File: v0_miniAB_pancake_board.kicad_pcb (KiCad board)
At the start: 2 copper layers, 51 x 38.3 mm, 17 parts, among them J1 E_STEPPER, J10 FAN0_V_JUMPER, J11 FAN1_V_JUMPER, J12 RGB LED, J13 BLTOUCH, J2 HEATER, J3 THERM, J4 PART FAN, J5 PART FAN, J6 HOTEND FAN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

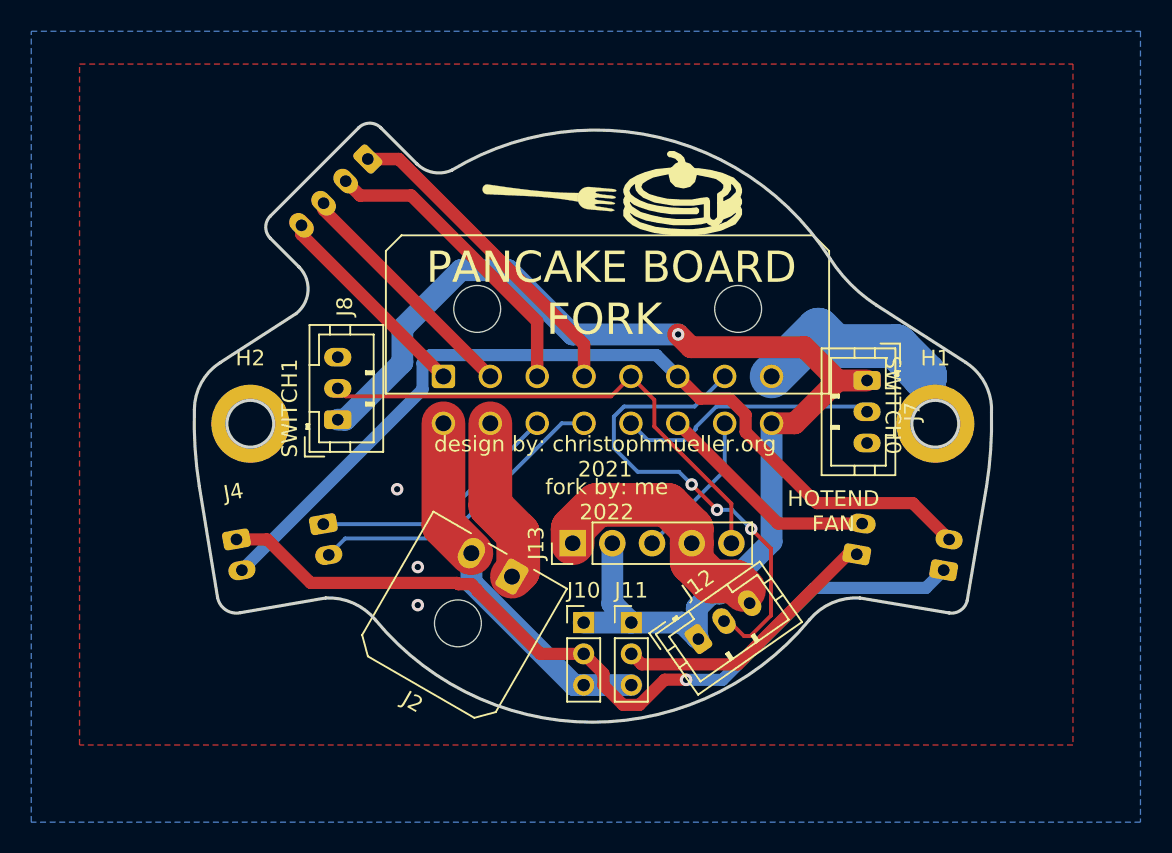
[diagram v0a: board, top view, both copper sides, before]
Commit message: Adjusted after comments
Fixed some pin orientations and pin assignments in the schematic.
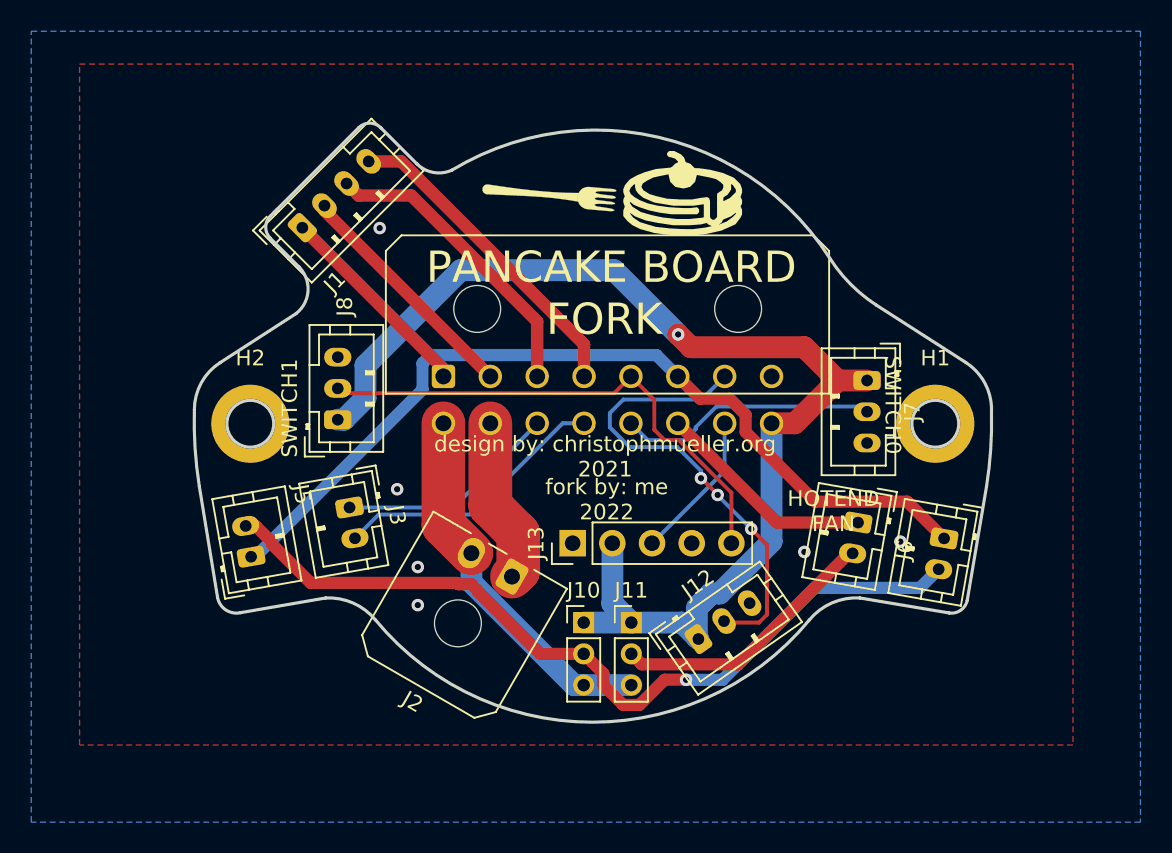
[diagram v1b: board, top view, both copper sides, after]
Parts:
- J1, J3, J4, J5, J6: moved to F.Cu
- J9: value Conn_02x07_Counter_Clockwise -> Breakout Molex Micro-fit 3.0 02x08
- moved J4 45.3 mm to (122.5, 107.3), turned to -100 degrees
- moved J5 44.3 mm to (78.1, 108.5), turned to 100 degrees
- moved J1 6.07 mm to (81.4, 87.5), turned to 45 degrees
- moved J6 2.03 mm to (117.0, 106.3), turned to -100 degrees
- moved J3 1.99 mm to (84.4, 105.4)
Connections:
- J1 pad 1: /B- -> /A+
- J1 pad 2: /B+ -> /A-
- J1 pad 3: /A- -> /B+
- J1 pad 4: /A+ -> /B-
- J4 pad 1: /VFAN0 -> /fan0
- J4 pad 2: /fan0 -> /VFAN0
- J5 pad 1: /VFAN0 -> /fan0
- J5 pad 2: /fan0 -> /VFAN0
- J6 pad 1: /VFAN1 -> /fan1
- J6 pad 2: /fan1 -> /VFAN1
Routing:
- net GND: track 31.2 -> 0.00 mm, vias 3 -> 6
- net /therm1: track 19.8 -> 17.7 mm
- net /therm0: track 16.4 -> 14.3 mm
- net /fan0: track 57.5 -> 56.5 mm
- net /led: track 31.1 -> 30.2 mm
- net +5V: track 76.8 -> 77.4 mm

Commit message: Add @famichu as co-designer
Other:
- board text added: "fork by: matthew & @famichu 2022"
- board text removed: "fork by: me 2022"
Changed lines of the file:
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@@
     (effects (font (size 2 2) (thickness 0.3)))
   )
-  (gr_text "fork by: me\n2022" (at 100.8888 104.8512) (layer "F.SilkS")
+  (gr_text "fork by: matthew & @famichu\n2022" (at 100.8888 104.8512) (layer "F.SilkS")
     (effects (font (size 1 1) (thickness 0.15)))
   )

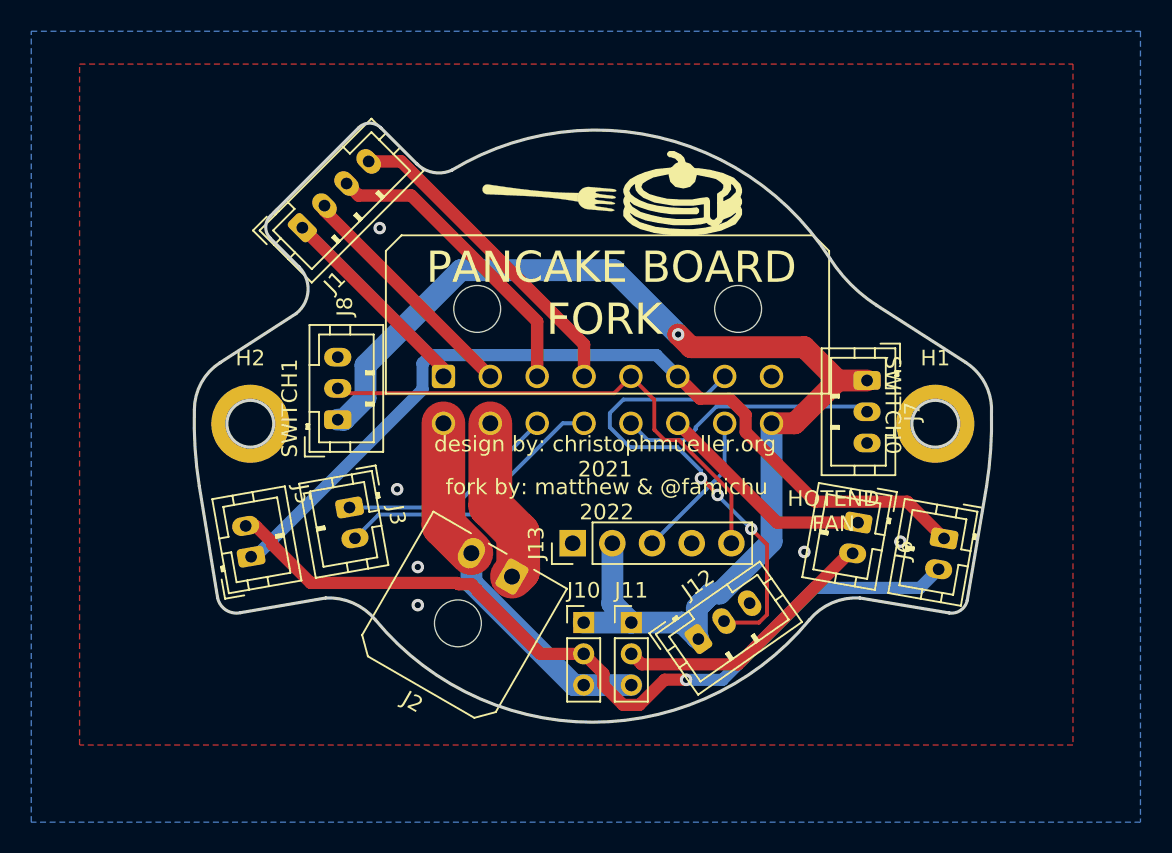
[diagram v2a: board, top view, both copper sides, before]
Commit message: Silkscreen changes
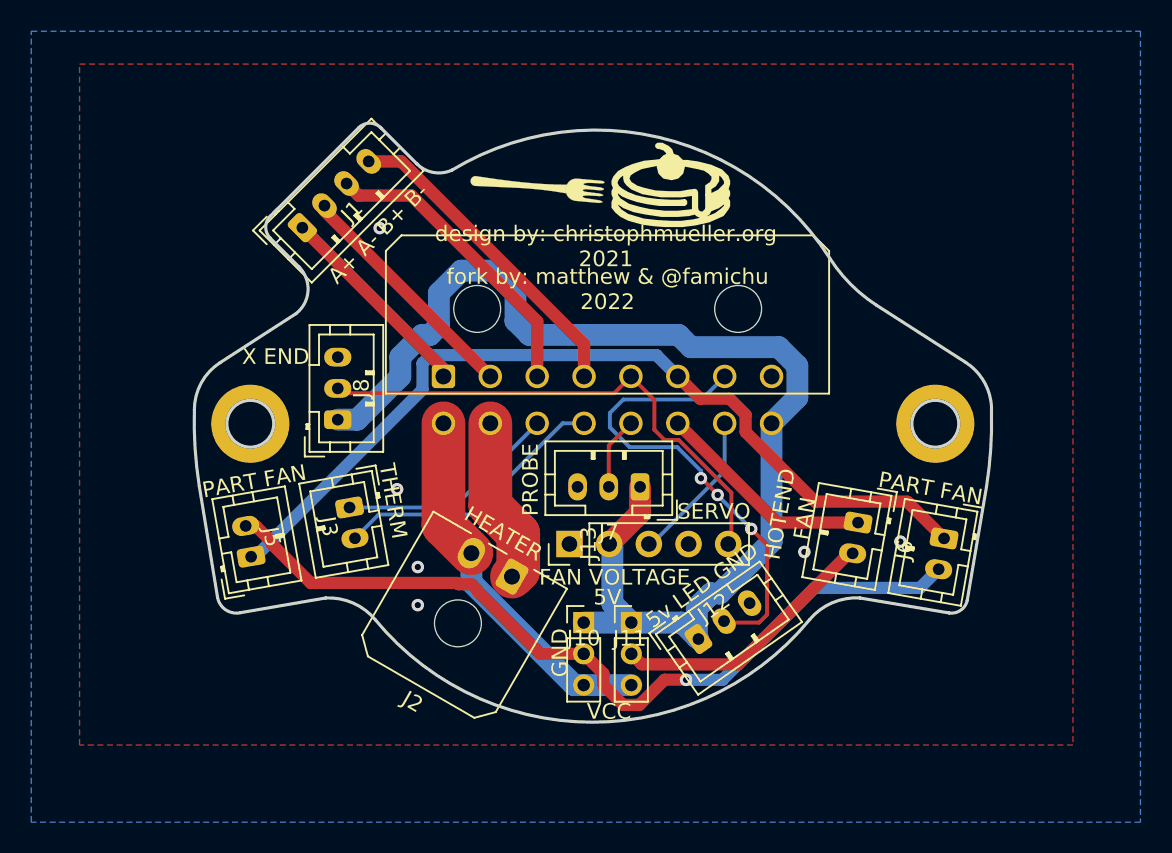
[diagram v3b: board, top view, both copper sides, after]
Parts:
- H1, H2: value MountingHole_Pad -> (none)
- J1: value E_STEPPER -> A+ A- B+ B-
- J10: value FAN0_V_JUMPER -> (none)
- J11: value FAN1_V_JUMPER -> (none)
- J12: value RGB LED -> (none)
- J2: value HEATER -> (none)
- J3: value THERM -> (none)
- J4, J5: value PART FAN -> (none)
- J6: value HOTEND FAN -> (none)
- J8: value ENDSTOP1 -> (none)
- moved J7 16.0 mm to (103.0, 104.0), turned to 180 degrees
- moved REF** 0.93 mm to (101.2, 88.5)
- moved J13 0.21 mm to (98.5, 107.7)
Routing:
- net /sw0: track 16.7 -> 4.65 mm
- net +5V: track 77.4 -> 77.8 mm, vias 1 -> 0
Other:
- board text added: "5V"
- board text added: "5v LED GND"
- board text added: "B- B+ A- A+"
- board text added: "FAN VOLTAGE"
- board text added: "GND"
- board text added: "PROBE"
- board text added: "SERVO"
- board text added: "THERM"
- board text added: "VCC"
- board text added: "X END"
- board text removed: "STEPPER"
- board text removed: "SWITCH0"
- board text removed: "SWITCH1"
